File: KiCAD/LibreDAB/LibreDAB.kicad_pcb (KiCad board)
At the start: 2 copper layers, 70 x 70 mm, 58 parts, among them J1 TS30050050-040, J2 TS30050050-040, J3 TS30050050-040, J4 TS30050050-040, J8 1x3 Socket header, Q1 SP010N01BGHTO, Q2 SP010N01BGHTO, Q3 SP010N01BGHTO, Q4 SP010N01BGHTO, U1 UCC27211DDAR, U2 UCC27211DDAR, U3 10 MHz Opamp, U4 10 MHz Opamp, U5 10 MHz Opamp

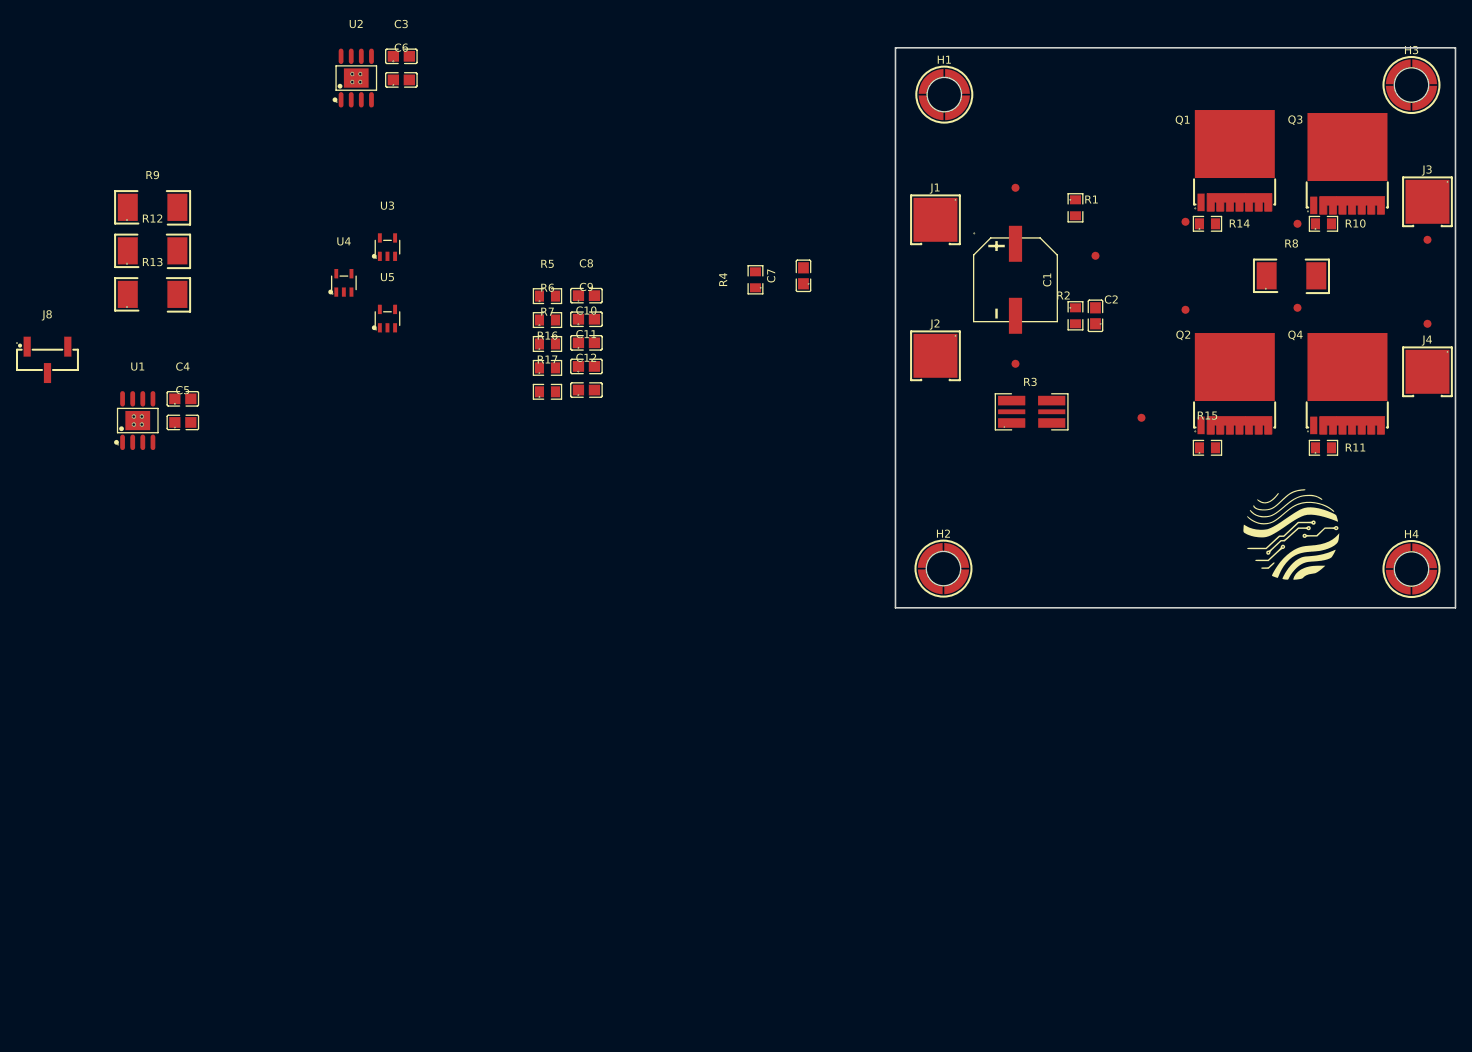
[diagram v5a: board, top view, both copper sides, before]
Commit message: PCB component placement on 92 x 92 mm board
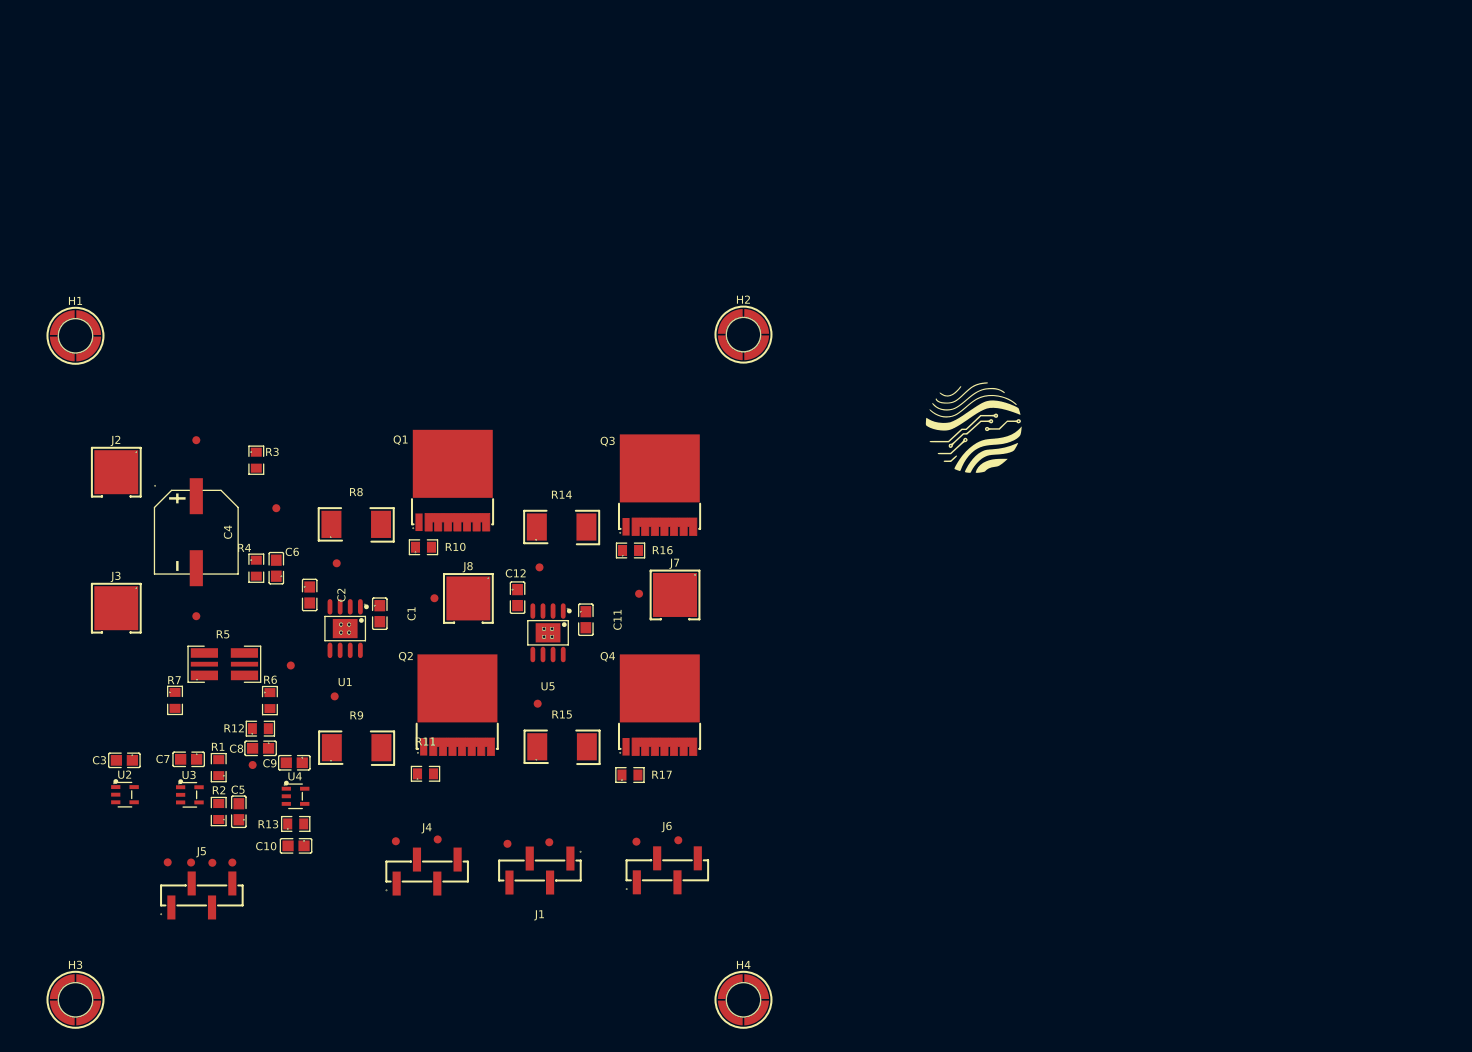
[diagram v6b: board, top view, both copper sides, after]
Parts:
- removed the J8 at (43.5, 89.5)
- added J1: HX PM2.54-1X4P TP H8.5-ZQ, lcsc_footprints:C48641754_HDR-SMD_4P-P2_54-V-F-LS4_7-R1, F.Cu at (105.1, 153.3)
- added J4: HX PM2.54-1X4P TP H8.5-ZQ, lcsc_footprints:C48641754_HDR-SMD_4P-P2_54-V-F-LS4_7-R1, F.Cu at (91.0, 153.5)
- added J5: HX PM2.54-1X4P TP H8.5-ZQ, lcsc_footprints:C48641754_HDR-SMD_4P-P2_54-V-F-LS4_7-R1, F.Cu at (62.8, 156.5)
- added J6: HX PM2.54-1X4P TP H8.5-ZQ, lcsc_footprints:C48641754_HDR-SMD_4P-P2_54-V-F-LS4_7-R1, F.Cu at (121.0, 153.3)
- added TP1: TestPoint_Probe, 1Footprints:TestPoint_Pad_D1.0mm, F.Cu at (106.2, 149.8)
- added TP11: TestPoint_Probe, 1Footprints:TestPoint_Pad_D1.0mm, F.Cu at (69.1, 140.1)
- added TP12: TestPoint_Probe, 1Footprints:TestPoint_Pad_D1.0mm, F.Cu at (122.4, 149.6)
- added TP18: TestPoint_Probe, 1Footprints:TestPoint_Pad_D1.0mm, F.Cu at (66.6, 152.3)
- added TP2: TestPoint_Probe, 1Footprints:TestPoint_Pad_D1.0mm, F.Cu at (87.0, 149.7)
- added TP20: TestPoint_Probe, 1Footprints:TestPoint_Pad_D1.0mm, F.Cu at (101.0, 150.0)
- added TP21: TestPoint_Probe, 1Footprints:TestPoint_Pad_D1.0mm, F.Cu at (64.1, 152.4)
- added TP3: TestPoint_Probe, 1Footprints:TestPoint_Pad_D1.0mm, F.Cu at (61.5, 152.3)
- added TP4: TestPoint_Probe, 1Footprints:TestPoint_Pad_D1.0mm, F.Cu at (58.5, 152.3)
- added TP7: TestPoint_Probe, 1Footprints:TestPoint_Pad_D1.0mm, F.Cu at (92.3, 149.5)
- added TP9: TestPoint_Probe, 1Footprints:TestPoint_Pad_D1.0mm, F.Cu at (117.1, 149.7)
- moved TP15 128.8 mm to (91.9, 119.3)
- moved J8 123.2 mm to (96.1, 119.3)
- moved H3 121.1 mm to (47.0, 169.5)
- moved TP14 116.8 mm to (79.4, 131.6)
- moved TP13 114.4 mm to (79.7, 114.9)
- moved H1 112.7 mm to (47.0, 86.5)
- moved TP10 110.8 mm to (73.9, 127.7)
- moved TP19 108.0 mm to (117.4, 118.7)
- moved C6 107.1 mm to (72.1, 115.5)
- moved R3 107.1 mm to (69.6, 102.0)
- moved R4 107.1 mm to (69.6, 115.5)
- moved TP8 107.1 mm to (72.1, 108.0)
- moved C4 107.1 mm to (62.1, 111.0)
- moved J2 107.1 mm to (52.1, 103.5)
- moved J3 107.1 mm to (52.1, 120.5)
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- renumbered C4 to C1, C11 to C10, C3 to C11, C6 to C12, C5 to C2, C9 to C3, C1 to C4, C7 to C5, C2 to C6, C8 to C7, C10 to C8, C12 to C9, H3 to H2, H2 to H3, J1 to J2, J2 to J3, J3 to J7, J4 to J8, R4 to R1, R14 to R10, R15 to R11, R16 to R12, R17 to R13, R8 to R14, R9 to R15, R10 to R16, R11 to R17, R5 to R2, R1 to R3, R2 to R4, R3 to R5, R12 to R8, R13 to R9, TP4 to TP10, TP7 to TP13, TP8 to TP14, TP6 to TP15, TP9 to TP16, TP10 to TP17, TP5 to TP19, TP1 to TP5, TP2 to TP6, TP3 to TP8, U3 to U2, U4 to U3, U5 to U4, U2 to U5
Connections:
- C1 pad 1: /LV_Bridge/Gate_Driver1/+12V -> +12V
- C1 pad 2: /LV_Bridge/Gate_Driver1/0 V -> GND
- C11 pad 1: /LV_Bridge/Gate_Driver2/+12V -> +12V
- C11 pad 2: /LV_Bridge/Gate_Driver2/0 V -> GND
- C3 pad 2: unconnected-(C9-Pad2) -> GND
- C8 pad 2: /LV_Bridge/V_LV- -> /LV_Bridge/Vref
- R12 pad 1: /LV_Bridge/V_LV- -> /LV_Bridge/Vref
- U1 pad 1: /LV_Bridge/Gate_Driver1/+12V -> +12V
- U1 pad 5: /LV_Bridge/Gate_Driver1/PWM-H -> /LV_Bridge/PWM-H1
- U1 pad 6: /LV_Bridge/Gate_Driver1/PWM-L -> /LV_Bridge/PWM-L1
- U1 pad 7: /LV_Bridge/Gate_Driver1/0 V -> GND
- U1 pad 9: unconnected-(U1-EP-Pad9) -> GND
- U3 pad 1: /LV_Bridge/V_LV- -> /LV_Bridge/Vref
- U3 pad 4: /LV_Bridge/V_LV- -> /LV_Bridge/Vref
- U5 pad 1: /LV_Bridge/Gate_Driver2/+12V -> +12V
- U5 pad 5: /LV_Bridge/Gate_Driver2/PWM-H -> /LV_Bridge/PWM-H2
- U5 pad 6: /LV_Bridge/Gate_Driver2/PWM-L -> /LV_Bridge/PWM-L2
- U5 pad 7: /LV_Bridge/Gate_Driver2/0 V -> GND
- U5 pad 9: unconnected-(U2-EP-Pad9) -> GND
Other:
- board outline removed

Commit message: Initial routing complete
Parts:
- LOGO1: moved to B.Cu
- moved LOGO1 73.9 mm to (89.6, 122.3), turned to 180 degrees
- moved C10 19.9 mm to (63.2, 133.9), turned to 0 degrees
- moved R13 16.1 mm to (63.2, 136.0), turned to 180 degrees
- moved J2 10.3 mm to (60.9, 98.1)
- moved J3 8.86 mm to (61.0, 120.5)
- moved R4 7.64 mm to (76.8, 112.9)
- moved C7 7.15 mm to (61.3, 146.6), turned to 0 degrees
- moved C3 7.02 mm to (53.2, 146.6), turned to 0 degrees
- moved C9 6.74 mm to (74.4, 146.6), turned to 0 degrees
- moved TP17 6.70 mm to (109.8, 128.1)
- moved TP14 6.66 mm to (85.0, 127.9)
- moved TP5 6.29 mm to (67.2, 117.8)
- moved R9 4.97 mm to (85.7, 134.5), turned to -90 degrees
- moved R3 4.91 mm to (74.2, 103.9)
- moved R15 4.85 mm to (111.3, 134.4), turned to -90 degrees
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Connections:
- R6 pad 1: GND -> /LV_Bridge/GND_sense
- R7 pad 1: /LV_Bridge/V_LV- -> /LV_Bridge/V_LV-_sense
- U1 pad : (no net) -> GND
- U5 pad : (no net) -> GND
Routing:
- net GND: track 0.00 -> 142.5 mm, vias 0 -> 18
- net +12V: track 0.00 -> 79.8 mm, vias 0 -> 3
- net /LV_Bridge/V_LV+: track 0.00 -> 69.3 mm
- net /LV_Bridge/V_LV_Divider: track 0.00 -> 57.2 mm, vias 0 -> 2
- net +5V: track 0.00 -> 56.3 mm
- net /LV_Bridge/LSW1: track 0.00 -> 52.2 mm, vias 0 -> 2
- net /LV_Bridge/LSW2: track 0.00 -> 51.4 mm, vias 0 -> 2
- net /LV_Bridge/I_LVsense: track 0.00 -> 39.1 mm, vias 0 -> 2
- net /LV_Bridge/PWM-L1: track 0.00 -> 37.6 mm, vias 0 -> 2
- net /LV_Bridge/PWM-L2: track 0.00 -> 37.0 mm, vias 0 -> 2
- net /LV_Bridge/PWM-H2: track 0.00 -> 35.3 mm, vias 0 -> 2
- net /LV_Bridge/PWM-H1: track 0.00 -> 34.0 mm, vias 0 -> 2
- net /LV_Bridge/V_LV-: track 0.00 -> 29.4 mm
- net /LV_Bridge/Vref: track 0.00 -> 22.8 mm
- net Net-(U4-IN-): track 0.00 -> 19.0 mm, vias 0 -> 2
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- added copper zone on F.Cu, net /LV_Bridge/V_LV-
- added copper zone on F.Cu, net GND
- added copper zone on In1.Cu, net GND
- added copper zone on In2.Cu, net GND
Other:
- board outline added: 92 x 92 mm
- copper layers 2 -> 4

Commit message: Started laying out power routing zones
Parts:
- moved R3 3.01 mm to (74.2, 106.9)
- moved TP8 1.65 mm to (74.2, 109.8)
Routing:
- net /LV_Bridge/V_LV_Divider: track 57.2 -> 50.4 mm
- net /LV_Bridge/V_LV+: vias 0 -> 32
- added copper zone on F.Cu, net /LV_Bridge/LSW1
- added copper zone on F.Cu, net /LV_Bridge/LSW2
- added copper zone on B.Cu, net /LV_Bridge/V_LV+
- added copper zone on F.Cu, net /LV_Bridge/V_LV+
- added copper zone on In1.Cu, net /LV_Bridge/V_LV+
- added copper zone on In2.Cu, net /LV_Bridge/V_LV+
